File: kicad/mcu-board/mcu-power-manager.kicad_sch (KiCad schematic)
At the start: 12 parts, among them J2 Conn_01x09_Pin, U1 AP3445LW6-7, U4 LM66200DRLR

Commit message: chore?: Saving again, might redo pcb
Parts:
- removed J2: Conn_01x09_Pin, Connector_PinHeader_2.54mm:PinHeader_1x09_P2.54mm_Vertical, symbol Connector:Conn_01x09_Pin
- added J13: Conn_01x06, Connector_PinHeader_2.54mm:PinHeader_1x06_P2.54mm_Vertical, symbol Connector_Generic:Conn_01x06
- L1: renamed from L2; footprint Inductor_SMD:L_1210_3225Metric -> PSAT_Library:IND_SPM6530T-1R5M100
- renumbered C7 to C3, C8 to C4, C11 to C5, C13 to C6, R12 to R7, R14 to R8, R7 to R9, U4 to U3, U1 to U4
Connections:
- net +3V3_PSU_FUSED: now also J13.1 (Pin_1)
- net +3V3_PSU_UNFUSED: now also J13.2 (Pin_2)
- net +5V_PSU_FUSED: now also J13.3 (Pin_3)
- net GND: now also J13.4 (Pin_4)
- net V_BAT/2: now also J13.5 (Pin_5)
- net V_USB: now also J13.6 (Pin_6)
- no-connect marks 2 -> 0

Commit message: chore: Fixed led footprint from 0805 to 0603, and edited title for buzzer
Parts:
- D1: footprint LED_SMD:LED_0805_2012Metric -> LED_SMD:LED_0603_1608Metric
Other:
- company: The Retrievers -> The Retrievers | Designed by aids
- title: (none) -> Power Management
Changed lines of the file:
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@@
 	(paper "A4")
 	(title_block
+		(title "Power Management")
 		(date "2025-12-10")
 		(rev "V1")
-		(company "The Retrievers")
+		(company "The Retrievers | Designed by aids")
 	)
 	(rectangle
@@
 			)
 		)
-		(property "Footprint" "LED_SMD:LED_0805_2012Metric"
+		(property "Footprint" "LED_SMD:LED_0603_1608Metric"
 			(at 264.16 54.61 0)
 			(effects

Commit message: fix: Fixed the mcu-board and preparing for the panelisation
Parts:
- added R12: 5.1k, Resistor_SMD:R_0805_2012Metric, symbol Device:R
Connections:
- net +3V3_OUT_UNFUSED: now also R12.1
- net POWER_ST: now also R12.2
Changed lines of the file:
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@@
 	)
 	(junction
+		(at 90.17 43.18)
+		(diameter 0)
+		(color 0 0 0 0)
+	)
+	(junction
 		(at 200.66 43.18)
 		(diameter 0)
@@
 	(wire
 		(pts
+			(xy 90.17 43.18) (xy 86.36 43.18)
+		)
+		(stroke
+			(width 0)
+			(type default)
+		)
+	)
+	(wire
+		(pts
 			(xy 259.08 64.77) (xy 259.08 67.31)
 		)
@@
 	(wire
 		(pts
-			(xy 96.52 43.18) (xy 86.36 43.18)
+			(xy 102.87 43.18) (xy 90.17 43.18)
 		)
 		(stroke
@@
 	)
 	(label "POWER_ST"
-		(at 96.52 43.18 180)
+		(at 102.87 43.18 180)
 		(effects
 			(font
@@
 	)
 	(symbol
+		(lib_id "power:+3V3")
+		(at 90.17 35.56 0)
+		(unit 1)
+		(exclude_from_sim no)
+		(in_bom yes)
+		(on_board yes)
+		(dnp no)
+		(property "Reference" "#PWR058"
+			(at 90.17 39.37 0)
+			(effects
+				(font
+					(size 1.27 1.27)
+				)
+				(hide yes)
+			)
+		)
+		(property "Value" "+3V3_OUT_UNFUSED"
+			(at 101.6 34.544 0)
+			(effects
+				(font
+					(size 1.27 1.27)
+				)
+			)
+		)
+		(property "Footprint" ""
+			(at 90.17 35.56 0)
+			(effects
+				(font
+					(size 1.27 1.27)
+				)
+				(hide yes)
+			)
+		)
+		(property "Datasheet" ""
+			(at 90.17 35.56 0)
+			(effects
+				(font
+					(size 1.27 1.27)
+				)
+				(hide yes)
+			)
+		)
+		(property "Description" "Power symbol creates a global label with name \"+3V3\""
+			(at 90.17 35.56 0)
+			(effects
+				(font
+					(size 1.27 1.27)
+				)
+				(hide yes)
+			)
+		)
+		(pin "1"
+		)
+		(instances
+			(project "mcu-board"
+				(path "/f6735569-a094-4d1f-804a-28898efbaebf/79b10459-455e-4cf2-8906-0ddec7d8d7a7"
+					(reference "#PWR058")
+					(unit 1)
+				)
+			)
+		)
+	)
+	(symbol
 		(lib_id "power:GND")
 		(at 231.14 46.99 90)
@@
 					(unit 1)
 				)
+			)
+		)
+	)
+	(symbol
+		(lib_id "Device:R")
+		(at 90.17 39.37 0)
+		(unit 1)
+		(exclude_from_sim no)
+		(in_bom yes)
+		(on_board yes)
+		(dnp no)
+		(property "Reference" "R12"
+			(at 87.63 39.37 90)
+			(effects
+				(font
+					(size 1.27 1.27)
+				)
+			)
+		)
+		(property "Value" "5.1k"
+			(at 90.424 39.37 90)
+			(effects
+				(font
+					(size 1.27 1.27)
+				)
+			)
+		)
+		(property "Footprint" "Resistor_SMD:R_0805_2012Metric"
+			(at 88.392 39.37 90)
+			(effects
+				(font
+					(size 1.27 1.27)
+				)
+				(hide yes)
+			)
+		)
+		(property "Datasheet" "~"
+			(at 90.17 39.37 0)
+			(effects
+				(font
+					(size 1.27 1.27)
+				)
+				(hide yes)
+			)
+		)
+		(property "Description" "Resistor"
+			(at 90.17 39.37 0)
+			(effects
+				(font
+					(size 1.27 1.27)
+				)
+				(hide yes)
+			)
+		)
+		(pin "1"
+		)
+		(pin "2"
+		)
+		(instances
+			(project "mcu-board"
+				(path "/f6735569-a094-4d1f-804a-28898efbaebf/79b10459-455e-4cf2-8906-0ddec7d8d7a7"
+					(reference "R12")
+					(unit 1)
+				)

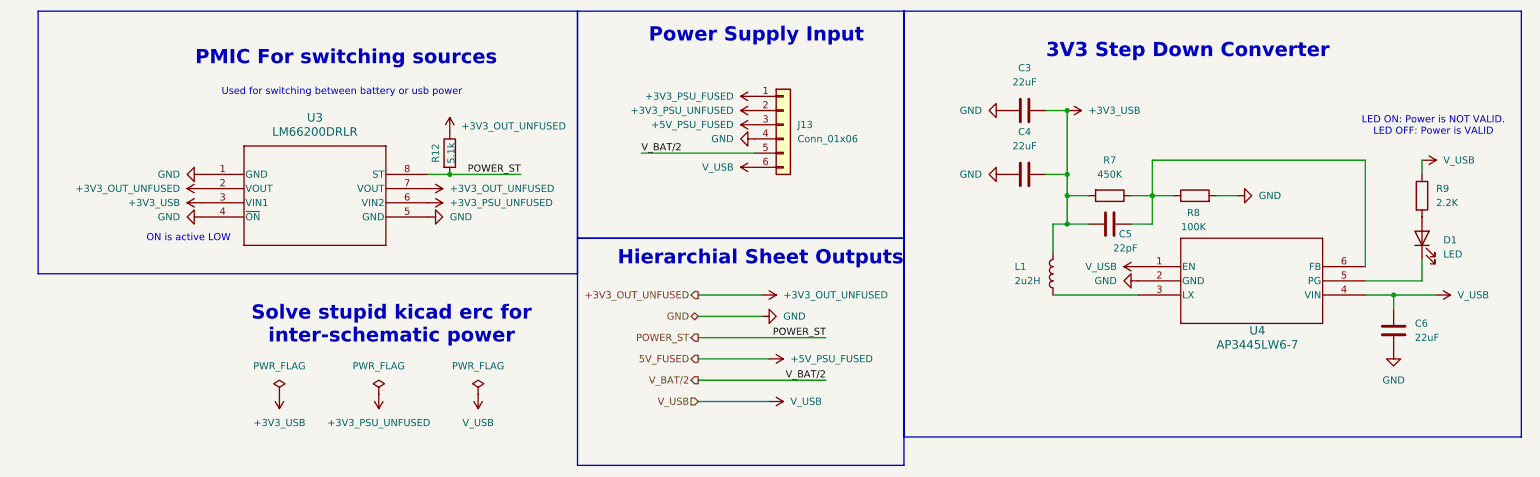
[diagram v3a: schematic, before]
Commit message: feat: finished v2 schematic of mcu-board
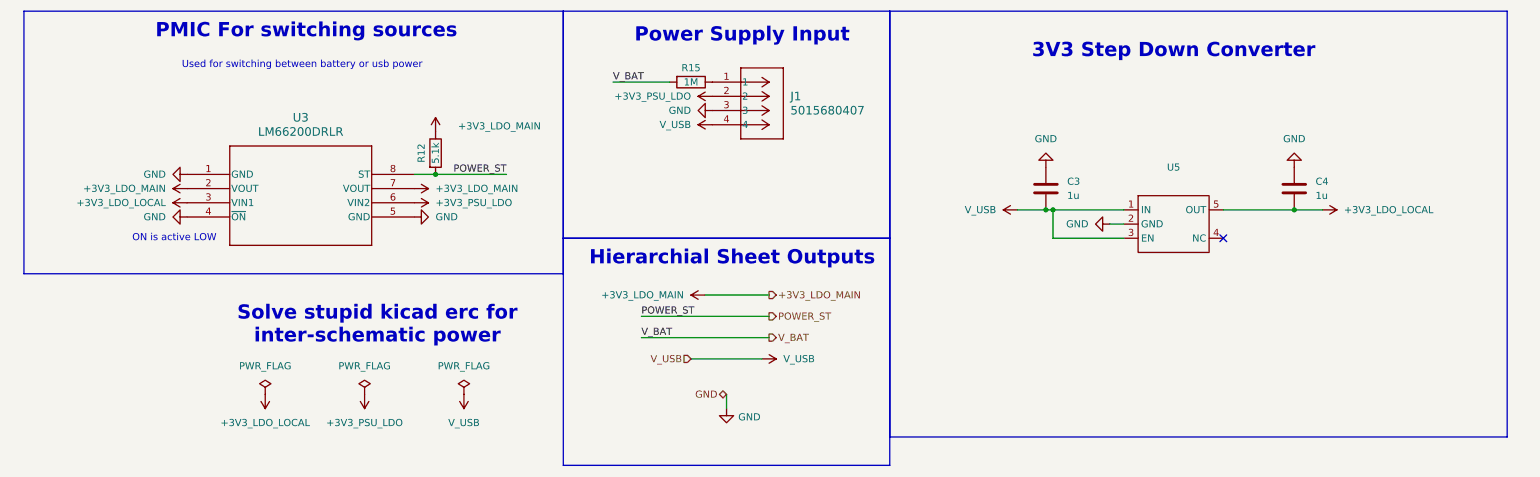
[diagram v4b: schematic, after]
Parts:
- removed C5: 22pF, Capacitor_SMD:C_0805_2012Metric, symbol Device:C
- removed C6: 22uF, Capacitor_SMD:C_0805_2012Metric, symbol Device:C
- removed D1: LED, LED_SMD:LED_0603_1608Metric, symbol Device:LED
- removed J13: Conn_01x06, Connector_PinHeader_2.54mm:PinHeader_1x06_P2.54mm_Vertical, symbol Connector_Generic:Conn_01x06
- removed L1: 2u2H, PSAT_Library:IND_SPM6530T-1R5M100, symbol Device:L
- removed R7: 450K, Resistor_SMD:R_0805_2012Metric, symbol Device:R
- removed R8: 100K, Resistor_SMD:R_0805_2012Metric, symbol Device:R
- removed R9: 2.2K, Resistor_SMD:R_0805_2012Metric, symbol Device:R
- removed U4: AP3445LW6-7, PSAT_Library:SOT26_AP3445_DIO-L, symbol 2025-11-28_22-50-25:AP3445LW6-7
- added J1: 5015680407, CONN_5015680000-SD_04_MOL, symbol 2026-01-26_05-30-52:5015680407
- added R15: 1M, Resistor_SMD:R_0805_2012Metric, symbol Device:R
- added U5: ~, TLV75733PDBVR:SOT-23-5_L2.9-W1.6-P0.95-LS2.8-BL, symbol PSAT_Library:TLV75733PDBVR
- C3, C4: value 22uF -> 1u; footprint Capacitor_SMD:C_0805_2012Metric -> (none)
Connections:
- net GND: now also J1.3, U5.2 (GND)
- net V_USB: now also C3.2, J1.4, U5.1 (IN), U5.3 (EN)
- net +3V3_OUT_UNFUSED renamed +3V3_LDO_MAIN
- net +3V3_PSU_UNFUSED renamed +3V3_PSU_LDO
- net +3V3_PSU_LDO: now also J1.2
- net +3V3_USB renamed +3V3_LDO_LOCAL
- net +3V3_LDO_LOCAL: now also U5.5 (OUT); no longer C3.2
- new net: J1.1, R15.1
- new net V_BAT: R15.2
- no-connect marks 0 -> 1
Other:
- note removed: "LED ON: Power is NOT VALID. LED OFF: Power is VALID"
- moved on the sheet: R12, U3

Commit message: feat: finished pcb, might add more artwork later?
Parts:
- removed J1: 5015680407, CONN_5015680000-SD_04_MOL, symbol 2026-01-26_05-30-52:5015680407
- removed R15: 1M, Resistor_SMD:R_0805_2012Metric, symbol Device:R
- added J7: 533980471, PSAT_Library:MOLEX_533980471, symbol PSAT_Library:533980471
- added TP21, TP22: TestPoint, TestPoint:TestPoint_Pad_D1.0mm, symbol Connector:TestPoint
- C8: renamed from C3; footprint (none) -> Capacitor_SMD:C_0805_2012Metric
- C9: renamed from C4; footprint (none) -> Capacitor_SMD:C_0805_2012Metric
- U3: footprint footprints:SOT-5X3_DRL_TEX -> footprints2:SOT-5X3_DRL_TEX
- U4: renamed from U5; value ~ -> TLV75733PDBVR; footprint TLV75733PDBVR:SOT-23-5_L2.9-W1.6-P0.95-LS2.8-BL -> footprints2:TLV75733PDBVR
- renumbered R12 to R8
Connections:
- net +3V3_LDO_LOCAL: now also R8.1, TP21.1
- net +3V3_LDO_MAIN: no longer R8.1
- net +3V3_PSU_LDO: now also J7.2, TP22.1
- net GND: now also J7.3
- net V_USB: now also J7.4
- new net VBAT_IO1: J7.1
- no-connect marks 1 -> 3
